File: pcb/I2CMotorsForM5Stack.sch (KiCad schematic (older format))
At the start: 18 parts, among them J1 free_holes, J3 Conn_01x06, J4 Conn_01x06, SW1 SW_DIP_x08, U1 TB6612FNG, U2 ATmega328PB-MU

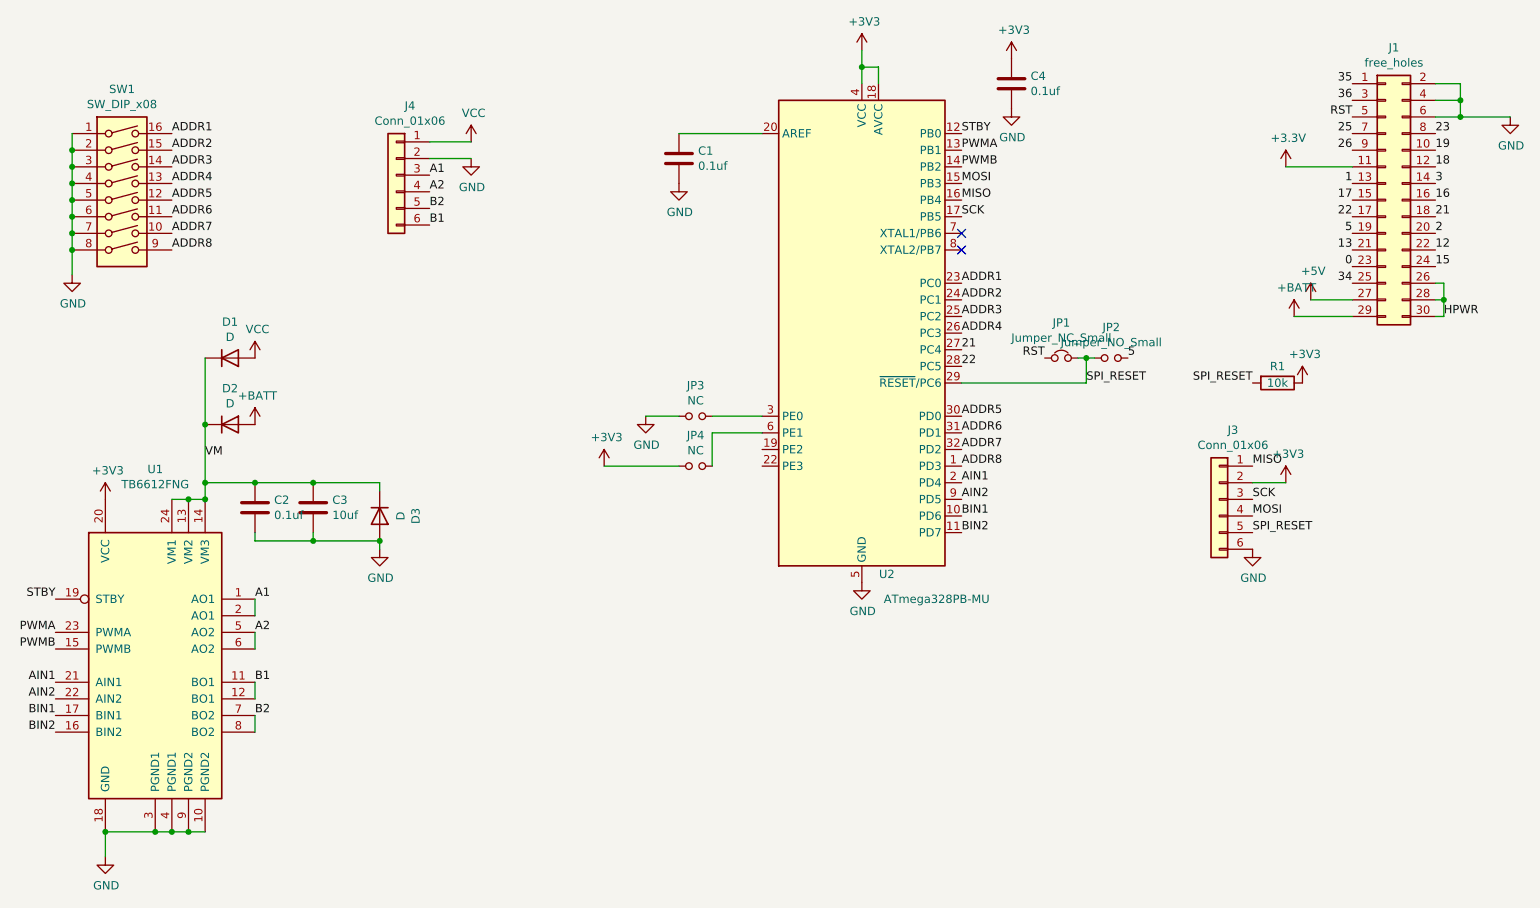
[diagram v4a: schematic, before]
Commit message: Add connectors and address pads
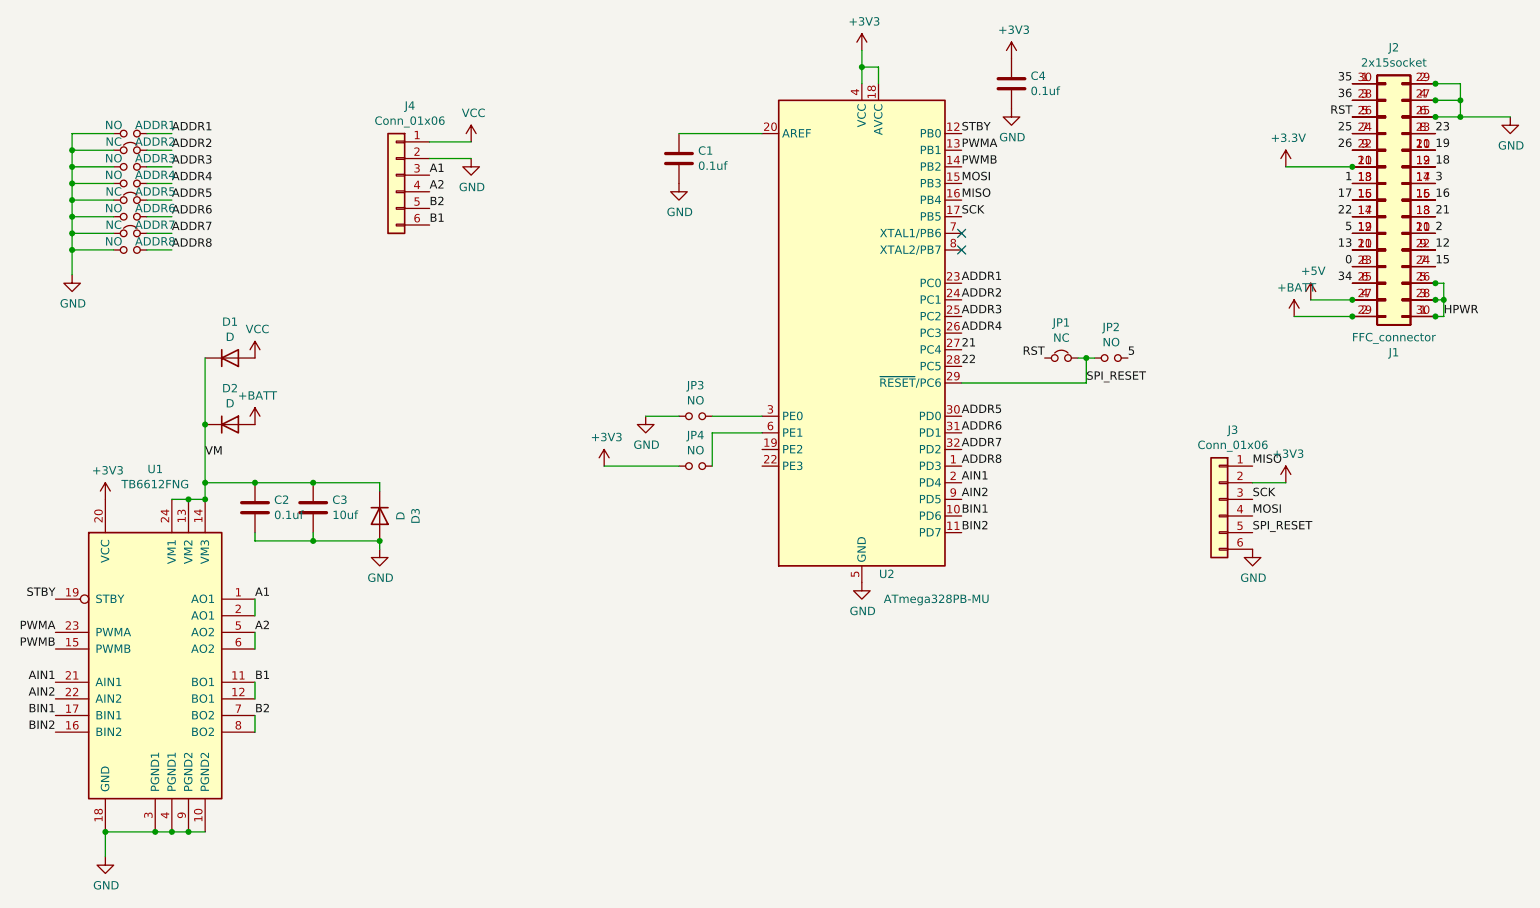
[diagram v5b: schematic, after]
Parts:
- removed R1: 10k, Resistor_SMD:R_0603_1608Metric, symbol Device:R
- removed SW1: SW_DIP_x08, Button_Switch_THT:SW_DIP_SPSTx08_Piano_CTS_Series194-8MSTN_W7.62mm_P2.54mm, symbol Switch:SW_DIP_x08
- added ADDR1, ADDR3, ADDR4, ADDR6, ADDR8: NO, Jumper:SolderJumper-2_P1.3mm_Open_RoundedPad1.0x1.5mm, symbol Device:Jumper_NO_Small
- added ADDR2, ADDR5, ADDR7: NC, Jumper:SolderJumper-2_P1.3mm_Bridged_RoundedPad1.0x1.5mm, symbol Device:Jumper_NC_Small
- added J2: 2x15socket, my-kicad-footprints:PinSocket_2x15_P2.54mm_Vertical_SMD_just_for_M5Stack_bottom, symbol Connector_Generic:Conn_02x15_Odd_Even
- J1: value free_holes -> FFC_connector; footprint footprints:Pads_1x30_P1.27mm_Vertical -> Connector_FFC-FPC:Hirose_FH12-30S-0.5SH_1x30-1MP_P0.50mm_Horizontal
- JP1: value Jumper_NC_Small -> NC
- JP2: value Jumper_NO_Small -> NO
- JP3, JP4: value NC -> NO
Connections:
- net +3V3: now also J1.20 (Pin_20), J2.11 (Pin_11); no longer J1.11 (Pin_11)
- net +5V: now also J1.4 (Pin_4), J2.27 (Pin_27); no longer J1.27 (Pin_27)
- net +BATT: now also J1.2 (Pin_2), J2.29 (Pin_29); no longer J1.29 (Pin_29)
- net 0: now also J1.8 (Pin_8), J2.23 (Pin_23); no longer J1.23 (Pin_23)
- net 1: now also J1.18 (Pin_18), J2.13 (Pin_13); no longer J1.13 (Pin_13)
- net 12: now also J1.9 (Pin_9), J2.22 (Pin_22); no longer J1.22 (Pin_22)
- net 13: now also J1.10 (Pin_10), J2.21 (Pin_21); no longer J1.21 (Pin_21)
- net 15: now also J1.7 (Pin_7), J2.24 (Pin_24); no longer J1.24 (Pin_24)
- net 16: now also J1.15 (Pin_15), J2.16 (Pin_16); no longer J1.16 (Pin_16)
- net 17: now also J1.16 (Pin_16), J2.15 (Pin_15); no longer J1.15 (Pin_15)
- net 18: now also J1.19 (Pin_19), J2.12 (Pin_12); no longer J1.12 (Pin_12)
- net 19: now also J1.21 (Pin_21), J2.10 (Pin_10); no longer J1.10 (Pin_10)
- net 2: now also J1.11 (Pin_11), J2.20 (Pin_20); no longer J1.20 (Pin_20)
- net 21: now also J1.13 (Pin_13), J2.18 (Pin_18); no longer J1.18 (Pin_18)
- net 22: now also J1.14 (Pin_14), J2.17 (Pin_17); no longer J1.17 (Pin_17)
- net 23: now also J1.23 (Pin_23), J2.8 (Pin_8); no longer J1.8 (Pin_8)
- net 25: now also J1.24 (Pin_24), J2.7 (Pin_7); no longer J1.7 (Pin_7)
- net 26: now also J1.22 (Pin_22), J2.9 (Pin_9); no longer J1.9 (Pin_9)
- net 3: now also J1.17 (Pin_17), J2.14 (Pin_14); no longer J1.14 (Pin_14)
- net 34: now also J1.6 (Pin_6), J2.25 (Pin_25); no longer J1.25 (Pin_25)
- net 35: now also J1.30 (Pin_30), J2.1 (Pin_1); no longer J1.1 (Pin_1)
- net 36: now also J1.28 (Pin_28), J2.3 (Pin_3); no longer J1.3 (Pin_3)
- net 5: now also J1.12 (Pin_12), J2.19 (Pin_19); no longer J1.19 (Pin_19)
- net ADDR1: now also ADDR1.2
- net ADDR2: now also ADDR2.2
- net ADDR3: now also ADDR3.2
- net ADDR4: now also ADDR4.2
- net ADDR5: now also ADDR5.2
- net ADDR6: now also ADDR6.2
- net ADDR7: now also ADDR7.2
- net ADDR8: now also ADDR8.2
- net GND: now also J1.25 (Pin_25), J1.27 (Pin_27), J1.29 (Pin_29), ADDR1.1, ADDR2.1, ADDR3.1, ADDR4.1, ADDR5.1, ADDR6.1, ADDR7.1, ADDR8.1, J2.2 (Pin_2), J2.4 (Pin_4), J2.6 (Pin_6); no longer J1.2 (Pin_2), J1.4 (Pin_4), J1.6 (Pin_6)
- net HPWR: now also J1.1 (Pin_1), J1.3 (Pin_3), J1.5 (Pin_5), J2.26 (Pin_26), J2.28 (Pin_28), J2.30 (Pin_30); no longer J1.26 (Pin_26), J1.28 (Pin_28), J1.30 (Pin_30)
- net RST: now also J1.26 (Pin_26), J2.5 (Pin_5); no longer J1.5 (Pin_5)
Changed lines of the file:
@@
 	1    0    0    -1
 $EndComp
-Wire Wire Line
-	10350 1800 10650 1800
 $Comp
 L Connector_Generic:Conn_02x15_Odd_Even J1
 U 1 1 5CD7CD4A
-P 9900 2300
-F 0 "J1" H 9950 3217 50  0000 C CNN
-F 1 "free_holes" H 9950 3126 50  0000 C CNN
-F 2 "footprints:Pads_1x30_P1.27mm_Vertical" H 9900 2300 50  0001 C CNN
-F 3 "~" H 9900 2300 50  0001 C CNN
-	1    9900 2300
-	1    0    0    -1
+P 10000 2300
+F 0 "J1" H 10050 3217 50  0000 C CNN
+F 1 "FFC_connector" H 10050 3126 50  0000 C CNN
+F 2 "Connector_FFC-FPC:Hirose_FH12-30S-0.5SH_1x30-1MP_P0.50mm_Horizontal" H 10000 2300 50  0001 C CNN
+F 3 "~" H 10000 2300 50  0001 C CNN
+	1    10000 2300
+	-1   0    0    1
 $EndComp
 $Comp
@@
 P 7950 3250
 F 0 "JP1" H 7950 3462 50  0000 C CNN
-F 1 "Jumper_NC_Small" H 7950 3371 50  0000 C CNN
+F 1 "NC" H 7950 3371 50  0000 C CNN
 F 2 "Jumper:SolderJumper-2_P1.3mm_Bridged_RoundedPad1.0x1.5mm" H 7950 3250 50  0001 C CNN
 F 3 "~" H 7950 3250 50  0001 C CNN
@@
 P 8250 3250
 F 0 "JP2" H 8250 3435 50  0000 C CNN
-F 1 "Jumper_NO_Small" H 8250 3344 50  0000 C CNN
+F 1 "NO" H 8250 3344 50  0000 C CNN
 F 2 "Jumper:SolderJumper-2_P1.3mm_Open_RoundedPad1.0x1.5mm" H 8250 3250 50  0001 C CNN
 F 3 "~" H 8250 3250 50  0001 C CNN
@@
 Text Label 9100 4100 0    50   ~ 0
 SCK
-Text Label 9100 3400 2    50   ~ 0
-SPI_RESET
-$Comp
-L Device:R R1
-U 1 1 5E44A165
-P 9250 3400
-F 0 "R1" V 9150 3400 50  0000 C CNN
-F 1 "10k" V 9250 3400 50  0000 C CNN
-F 2 "Resistor_SMD:R_0603_1608Metric" V 9180 3400 50  0001 C CNN
-F 3 "~" H 9250 3400 50  0001 C CNN
-	1    9250 3400
-	0    1    1    0
-$EndComp
-$Comp
-L power:+3V3 #PWR0116
-U 1 1 5E44B3D6
-P 9400 3400
-F 0 "#PWR0116" H 9400 3250 50  0001 C CNN
-F 1 "+3V3" H 9415 3573 50  0000 C CNN
-F 2 "" H 9400 3400 50  0001 C CNN
-F 3 "" H 9400 3400 50  0001 C CNN
-	1    9400 3400
-	1    0    0    -1
-$EndComp
 Text Label 7350 4000 0    50   ~ 0
 AIN1
@@
 ADDR2
 $Comp
-L Switch:SW_DIP_x08 SW1
-U 1 1 5E665E4B
-P 2300 2300
-F 0 "SW1" H 2300 2967 50  0000 C CNN
-F 1 "SW_DIP_x08" H 2300 2876 50  0000 C CNN
-F 2 "Button_Switch_THT:SW_DIP_SPSTx08_Piano_CTS_Series194-8MSTN_W7.62mm_P2.54mm" H 2300 2300 50  0001 C CNN
-F 3 "~" H 2300 2300 50  0001 C CNN
-	1    2300 2300
-	1    0    0    -1
-$EndComp
-$Comp
 L power:GND #PWR0117
 U 1 1 5E66647B
@@
 	1    0    0    -1
 $EndComp
-Wire Wire Line
-	2000 2750 2000 2600
-Connection ~ 2000 2000
-Wire Wire Line
-	2000 2000 2000 1900
-Connection ~ 2000 2100
-Wire Wire Line
-	2000 2100 2000 2000
-Connection ~ 2000 2200
-Wire Wire Line
-	2000 2200 2000 2100
-Connection ~ 2000 2300
-Wire Wire Line
-	2000 2300 2000 2200
-Connection ~ 2000 2400
-Wire Wire Line
-	2000 2400 2000 2300
-Connection ~ 2000 2500
-Wire Wire Line
-	2000 2500 2000 2400
-Connection ~ 2000 2600
-Wire Wire Line
-	2000 2600 2000 2500
 Text Label 7350 3000 0    50   ~ 0
 ADDR3
@@
 P 5750 3600
 F 0 "JP3" H 5750 3785 50  0000 C CNN
-F 1 "NC" H 5750 3694 50  0000 C CNN
+F 1 "NO" H 5750 3694 50  0000 C CNN
 F 2 "Jumper:SolderJumper-2_P1.3mm_Open_RoundedPad1.0x1.5mm" H 5750 3600 50  0001 C CNN
 F 3 "~" H 5750 3600 50  0001 C CNN
@@
 P 5750 3900
 F 0 "JP4" H 5750 4085 50  0000 C CNN
-F 1 "NC" H 5750 3994 50  0000 C CNN
+F 1 "NO" H 5750 3994 50  0000 C CNN
 F 2 "Jumper:SolderJumper-2_P1.3mm_Open_RoundedPad1.0x1.5mm" H 5750 3900 50  0001 C CNN
 F 3 "~" H 5750 3900 50  0001 C CNN
@@
 Text Label 2800 3850 0    50   ~ 0
 VM
+Connection ~ 9700 2100
+Connection ~ 10200 1600
+Connection ~ 10200 2800
+Connection ~ 9700 2900
+Connection ~ 10200 2900
+Connection ~ 9700 3000
+Connection ~ 10200 3000
+Connection ~ 10200 1700
+Connection ~ 10200 1800
+Wire Wire Line
+	10350 1800 10650 1800
+$Comp
+L Connector_Generic:Conn_02x15_Odd_Even J2
+U 1 1 5E839DF5
+P 9900 2300
+F 0 "J2" H 9950 3217 50  0000 C CNN
+F 1 "2x15socket" H 9950 3126 50  0000 C CNN
+F 2 "my-kicad-footprints:PinSocket_2x15_P2.54mm_Vertical_SMD_just_for_M5Stack_bottom" H 9900 2300 50  0001 C CNN
+F 3 "~" H 9900 2300 50  0001 C CNN
+	1    9900 2300
+	1    0    0    -1
+$EndComp
+$Comp
+L Device:Jumper_NC_Small ADDR2
+U 1 1 5E84FB49
+P 2350 2000
+F 0 "ADDR2" H 2500 2050 50  0000 C CNN
+F 1 "NC" H 2250 2050 50  0000 C CNN
+F 2 "Jumper:SolderJumper-2_P1.3mm_Bridged_RoundedPad1.0x1.5mm" H 2350 2000 50  0001 C CNN
+F 3 "~" H 2350 2000 50  0001 C CNN
+	1    2350 2000
+	1    0    0    -1
+$EndComp
+$Comp
+L Device:Jumper_NO_Small ADDR1
+U 1 1 5E8501F7
+P 2350 1900
+F 0 "ADDR1" H 2500 1950 50  0000 C CNN
+F 1 "NO" H 2250 1950 50  0000 C CNN
+F 2 "Jumper:SolderJumper-2_P1.3mm_Open_RoundedPad1.0x1.5mm" H 2350 1900 50  0001 C CNN
+F 3 "~" H 2350 1900 50  0001 C CNN
+	1    2350 1900
+	1    0    0    -1
+$EndComp
+Wire Wire Line
+	2000 1900 2000 2000
+$Comp
+L Device:Jumper_NO_Small ADDR3
+U 1 1 5E855E5F
+P 2350 2100
+F 0 "ADDR3" H 2500 2150 50  0000 C CNN
+F 1 "NO" H 2250 2150 50  0000 C CNN
+F 2 "Jumper:SolderJumper-2_P1.3mm_Open_RoundedPad1.0x1.5mm" H 2350 2100 50  0001 C CNN
+F 3 "~" H 2350 2100 50  0001 C CNN
+	1    2350 2100
+	1    0    0    -1
+$EndComp
+$Comp
+L Device:Jumper_NO_Small ADDR4
+U 1 1 5E855FAF
+P 2350 2200
+F 0 "ADDR4" H 2500 2250 50  0000 C CNN
+F 1 "NO" H 2250 2250 50  0000 C CNN
+F 2 "Jumper:SolderJumper-2_P1.3mm_Open_RoundedPad1.0x1.5mm" H 2350 2200 50  0001 C CNN
+F 3 "~" H 2350 2200 50  0001 C CNN
+	1    2350 2200
+	1    0    0    -1
+$EndComp
+$Comp
+L Device:Jumper_NC_Small ADDR5
+U 1 1 5E8560B1
+P 2350 2300
+F 0 "ADDR5" H 2500 2350 50  0000 C CNN
+F 1 "NC" H 2250 2350 50  0000 C CNN
+F 2 "Jumper:SolderJumper-2_P1.3mm_Bridged_RoundedPad1.0x1.5mm" H 2350 2300 50  0001 C CNN
+F 3 "~" H 2350 2300 50  0001 C CNN
+	1    2350 2300
+	1    0    0    -1
+$EndComp
+$Comp
+L Device:Jumper_NO_Small ADDR6
+U 1 1 5E856295
+P 2350 2400
+F 0 "ADDR6" H 2500 2450 50  0000 C CNN
+F 1 "NO" H 2250 2450 50  0000 C CNN
+F 2 "Jumper:SolderJumper-2_P1.3mm_Open_RoundedPad1.0x1.5mm" H 2350 2400 50  0001 C CNN
+F 3 "~" H 2350 2400 50  0001 C CNN
+	1    2350 2400
+	1    0    0    -1
+$EndComp
+$Comp
+L Device:Jumper_NC_Small ADDR7
+U 1 1 5E856411
+P 2350 2500
+F 0 "ADDR7" H 2500 2550 50  0000 C CNN
+F 1 "NC" H 2250 2550 50  0000 C CNN
+F 2 "Jumper:SolderJumper-2_P1.3mm_Bridged_RoundedPad1.0x1.5mm" H 2350 2500 50  0001 C CNN
+F 3 "~" H 2350 2500 50  0001 C CNN
+	1    2350 2500
+	1    0    0    -1
+$EndComp
+$Comp
+L Device:Jumper_NO_Small ADDR8
+U 1 1 5E8565AF
+P 2350 2600
+F 0 "ADDR8" H 2500 2650 50  0000 C CNN
+F 1 "NO" H 2250 2650 50  0000 C CNN
+F 2 "Jumper:SolderJumper-2_P1.3mm_Open_RoundedPad1.0x1.5mm" H 2350 2600 50  0001 C CNN
+F 3 "~" H 2350 2600 50  0001 C CNN
+	1    2350 2600
+	1    0    0    -1
+$EndComp
+Wire Wire Line
+	2600 1900 2450 1900
+Wire Wire Line
+	2250 1900 2000 1900
+Wire Wire Line
+	2000 2000 2250 2000
+Connection ~ 2000 2000
+Wire Wire Line
+	2000 2000 2000 2100
+Wire Wire Line
+	2450 2000 2600 2000
+Wire Wire Line
+	2600 2100 2450 2100
+Wire Wire Line
+	2250 2100 2000 2100
+Connection ~ 2000 2100
+Wire Wire Line
+	2000 2100 2000 2200
+Wire Wire Line
+	2000 2200 2250 2200
+Connection ~ 2000 2200
+Wire Wire Line
+	2000 2200 2000 2300
+Wire Wire Line
+	2450 2200 2600 2200
+Wire Wire Line
+	2600 2300 2450 2300
+Wire Wire Line
+	2250 2300 2000 2300
+Connection ~ 2000 2300
+Wire Wire Line
+	2000 2300 2000 2400
+Wire Wire Line
+	2000 2400 2250 2400
+Connection ~ 2000 2400
+Wire Wire Line
+	2000 2400 2000 2500
+Wire Wire Line
+	2450 2400 2600 2400
+Wire Wire Line
+	2600 2500 2450 2500
+Wire Wire Line
+	2250 2500 2000 2500
+Connection ~ 2000 2500
+Wire Wire Line
+	2000 2500 2000 2600
+Wire Wire Line
+	2000 2600 2250 2600
+Connection ~ 2000 2600
+Wire Wire Line
+	2000 2600 2000 2750
+Wire Wire Line
+	2450 2600 2600 2600
 $EndSCHEMATC
